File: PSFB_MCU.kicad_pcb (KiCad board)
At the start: 6 copper layers, 38.5 x 33 mm, 104 parts, among them J2 2-215079-0, J3 Conn_01x16, J4 Conn_01x16, U1 APM32F405RGT6, U10 LMV321, U11 LMV321, U12 FM25W256, U13 LMV321, U14 LMV321, U15 LMV321, U16 LMV321, U2 LM2594HVM-3.3, Y1 CSTCE8M00G55A-R0

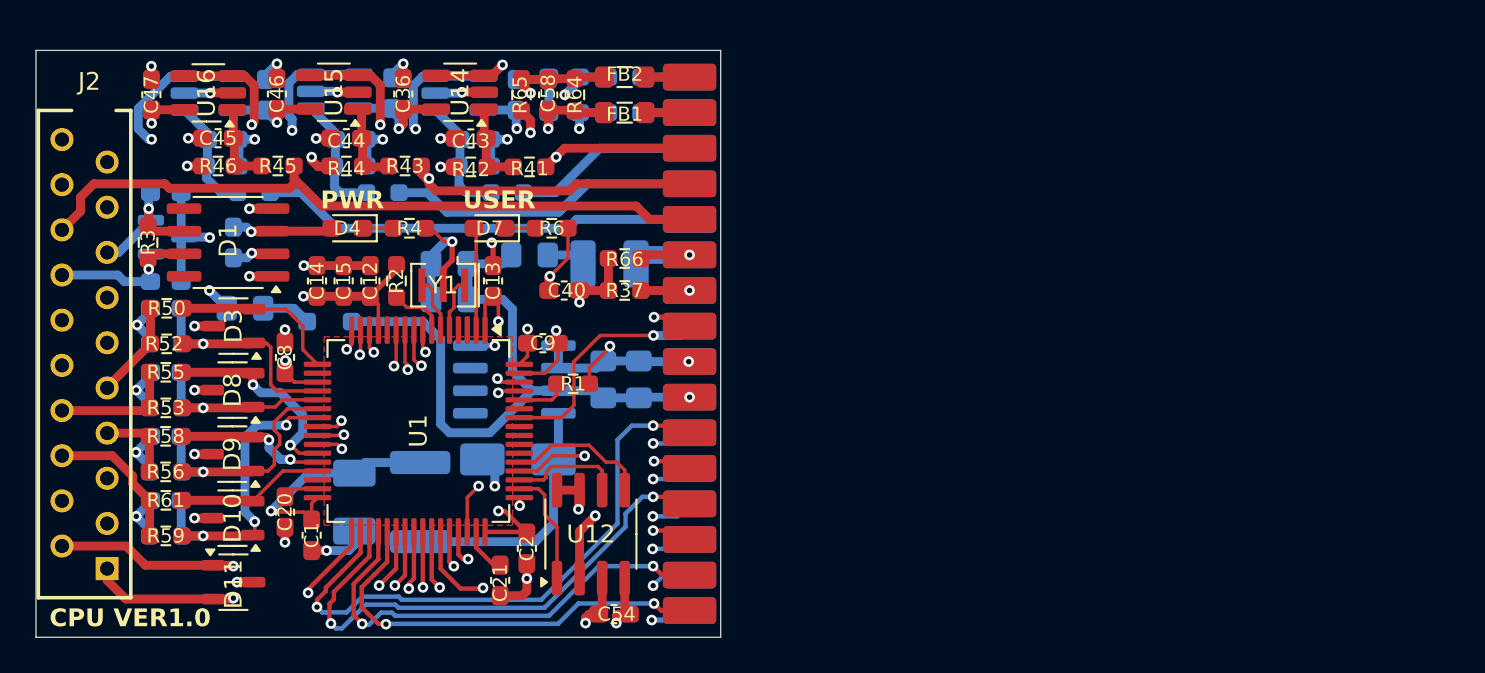
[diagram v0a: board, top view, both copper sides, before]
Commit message: VER1.0: убрал лишнее, добавил на схему питание 5В
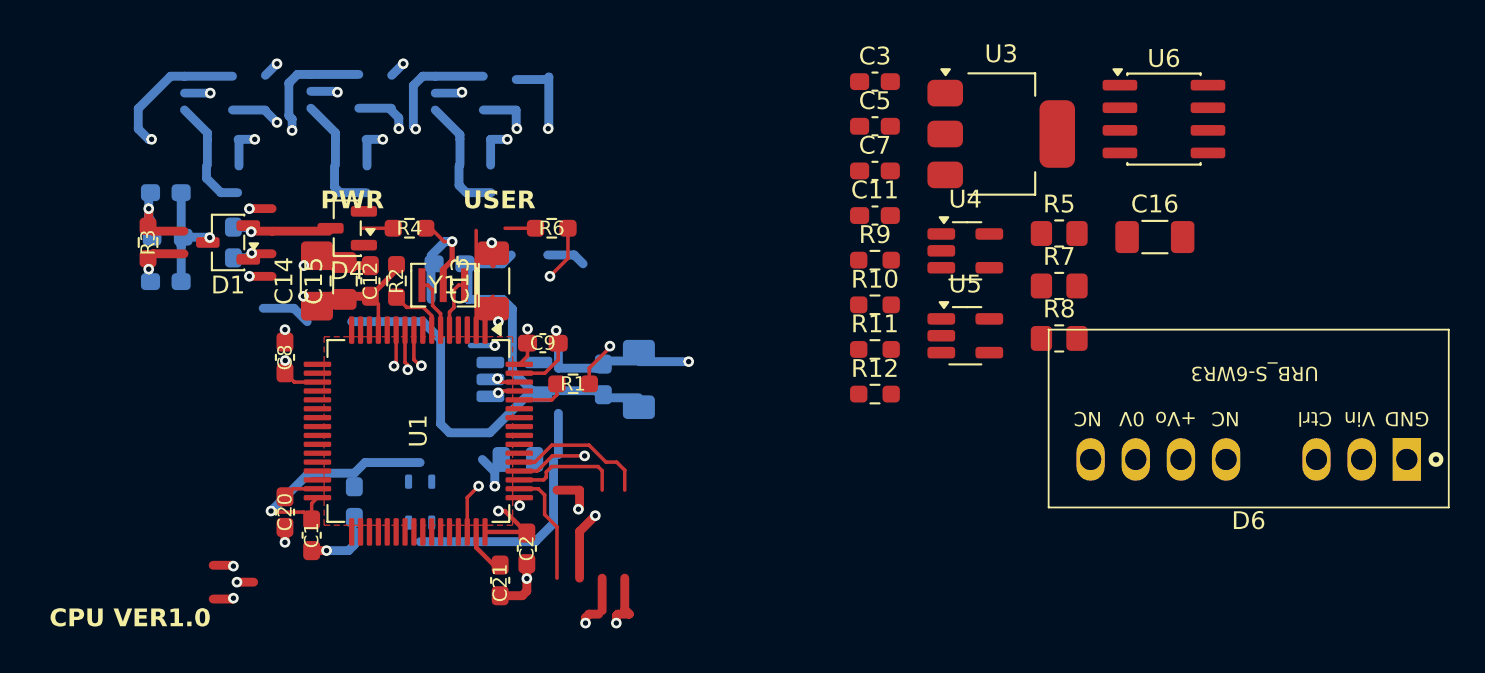
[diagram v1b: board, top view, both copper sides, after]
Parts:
- removed C23: 10u, Capacitor_SMD:C_0805_2012Metric_Pad1.18x1.45mm_HandSolder
- removed C33, C34, C35, C36, C46, C47, C51, C52, C53, C55, C56, C57: 100n, Capacitor_SMD:C_0603_1608Metric_Pad1.08x0.95mm_HandSolder
- removed C37, C39, C40, C41, C43, C44, C45: 1n, Capacitor_SMD:C_0603_1608Metric_Pad1.08x0.95mm_HandSolder
- removed C54: 1u, Capacitor_SMD:C_0603_1608Metric_Pad1.08x0.95mm_HandSolder
- removed C58: 2.2u, Capacitor_SMD:C_0603_1608Metric_Pad1.08x0.95mm_HandSolder
- removed D10, D11, D3, D8, D9: GSOT03C-E3-08, Package_TO_SOT_SMD:SOT-23-3
- removed D7: ~, LED_SMD:LED_0603_1608Metric_Pad1.05x0.95mm_HandSolder
- removed F1, F2: Fuse_Small, Fuse:Fuse_0805_2012Metric_Pad1.15x1.40mm_HandSolder
- removed FB1, FB2: BLM21AG102SN1D, Inductor_SMD:L_0805_2012Metric_Pad1.05x1.20mm_HandSolder
- removed J2: 2-215079-0, TE_my:22150790
- removed J3, J4: Conn_01x16, PLD_my:PLD16_2.0mm
- removed L2: 2.2u, Inductor_SMD:L_1210_3225Metric_Pad1.42x2.65mm_HandSolder
- removed R32, R35, R38, R41, R43, R45, R50, R52, R53, R55, R56, R58, R59, R61, R65: 1.8k, Resistor_SMD:R_0603_1608Metric_Pad0.98x0.95mm_HandSolder
- removed R34, R36, R37, R39, R42, R44, R46, R51, R54, R57, R60, R62, R63, R66: 3.6k, Resistor_SMD:R_0603_1608Metric_Pad0.98x0.95mm_HandSolder
- removed R64: 3.3k, Resistor_SMD:R_0603_1608Metric_Pad0.98x0.95mm_HandSolder
- removed U10, U11, U13, U14, U15, U16: LMV321, Package_TO_SOT_SMD:SOT-23-5_HandSoldering
- removed U12: FM25W256, Package_SO:SOIC-8_3.9x4.9mm_P1.27mm
- added C11: 100n, Capacitor_SMD:C_0603_1608Metric_Pad1.08x0.95mm_HandSolder, F.Cu at (173.7, 91.8)
- added C16: 10u, Capacitor_SMD:C_1206_3216Metric_Pad1.33x1.80mm_HandSolder, F.Cu at (189.4, 93.0)
- added C3: 100n, Capacitor_SMD:C_0603_1608Metric_Pad1.08x0.95mm_HandSolder, F.Cu at (173.7, 84.3)
- added C5: 100n, Capacitor_SMD:C_0603_1608Metric_Pad1.08x0.95mm_HandSolder, F.Cu at (173.7, 86.8)
- added C7: 4.7u, Capacitor_SMD:C_0603_1608Metric_Pad1.08x0.95mm_HandSolder, F.Cu at (173.7, 89.3)
- added R10: 3.6k, Resistor_SMD:R_0603_1608Metric_Pad0.98x0.95mm_HandSolder, F.Cu at (173.7, 96.8)
- added R11: 1.8k, Resistor_SMD:R_0603_1608Metric_Pad0.98x0.95mm_HandSolder, F.Cu at (173.7, 99.3)
- added R12: 3.6k, Resistor_SMD:R_0603_1608Metric_Pad0.98x0.95mm_HandSolder, F.Cu at (173.7, 101.8)
- added R5: 59, Resistor_SMD:R_0805_2012Metric_Pad1.20x1.40mm_HandSolder, F.Cu at (184.0, 92.8)
- added R7: 59, Resistor_SMD:R_0805_2012Metric_Pad1.20x1.40mm_HandSolder, F.Cu at (184.0, 95.7)
- added R8: 750, Resistor_SMD:R_0805_2012Metric_Pad1.20x1.40mm_HandSolder, F.Cu at (184.0, 98.7)
- added R9: 1.8k, Resistor_SMD:R_0603_1608Metric_Pad0.98x0.95mm_HandSolder, F.Cu at (173.7, 94.3)
- added U3: TLV1117LV33DCYR, Package_TO_SOT_SMD:SOT-223-3_TabPin2, F.Cu at (180.8, 87.2)
- added U4: ~, Package_TO_SOT_SMD:SOT-23-5_HandSoldering, F.Cu at (178.8, 93.8)
- added U5: ~, Package_TO_SOT_SMD:SOT-23-5_HandSoldering, F.Cu at (178.8, 98.5)
- added U6: ~, Package_SO:SOIC-8_3.9x4.9mm_P1.27mm, F.Cu at (189.9, 86.4)
- C10: value 56p -> 2.2u
- C12: value 100n -> 1n
- C13: value 100n -> 10u; footprint Capacitor_SMD:C_0603_1608Metric_Pad1.08x0.95mm_HandSolder -> Capacitor_SMD:C_1206_3216Metric_Pad1.33x1.80mm_HandSolder
- C14: value 4.7u -> 0.1u; footprint Capacitor_SMD:C_0603_1608Metric_Pad1.08x0.95mm_HandSolder -> Capacitor_SMD:C_1206_3216Metric_Pad1.33x1.80mm_HandSolder
- C15: value 1u -> 10n; footprint Capacitor_SMD:C_0603_1608Metric_Pad1.08x0.95mm_HandSolder -> Capacitor_SMD:C_0805_2012Metric_Pad1.18x1.45mm_HandSolder
- C17: footprint Capacitor_SMD:C_0805_2012Metric_Pad1.18x1.45mm_HandSolder -> Capacitor_SMD:C_1206_3216Metric_Pad1.33x1.80mm_HandSolder
- C18: value 10u -> 100n; footprint Capacitor_SMD:C_0805_2012Metric_Pad1.18x1.45mm_HandSolder -> Capacitor_SMD:C_0603_1608Metric_Pad1.08x0.95mm_HandSolder
- C19: value 100u -> 1n; footprint Capacitor_Tantalum_SMD:CP_EIA-3528-21_Kemet-B_HandSolder -> Capacitor_SMD:C_0603_1608Metric_Pad1.08x0.95mm_HandSolder
- C20, C6: value 2.2u -> 100n
- C21: value 2.2u -> 1n
- C22: value 10u -> 1u; footprint Capacitor_SMD:C_0805_2012Metric_Pad1.18x1.45mm_HandSolder -> Capacitor_SMD:C_0603_1608Metric_Pad1.08x0.95mm_HandSolder
- C4: value 56p -> 100n
- C8: value 100n -> 1u
- C9: value 100n -> 2.2u
- D1: footprint Package_SO:SOIC-8_3.9x4.9mm_P1.27mm -> Package_TO_SOT_SMD:SOT-23-3
- D2: footprint Package_TO_SOT_SMD:SOT-23 -> LED_SMD:LED_0603_1608Metric_Pad1.05x0.95mm_HandSolder
- D4: footprint LED_SMD:LED_0603_1608Metric_Pad1.05x0.95mm_HandSolder -> Package_TO_SOT_SMD:SOT-23
- D5: value MBRA320 -> ~; footprint Diode_SMD:D_SMA -> LED_SMD:LED_0805_2012Metric
- D6: value D_Schottky_Small -> ~; footprint Diode_SMD:D_SOD-323_HandSoldering -> MORNSUN:URB_S-6WR3; moved to F.Cu
- L1: value 47u -> ~; footprint Inductor_SMD:L_1812_4532Metric_Pad1.30x3.40mm_HandSolder -> Inductor_SMD:L_CommonModeChoke_TDK_ACM2520-2P
- R3: value 120 -> 1k
- R4: value 750 -> 1.8k
- R6: value 1k -> 3.6k
- U1: value APM32F405RGT6 -> ~
- U2: value LM2594HVM-3.3 -> ~; footprint Package_SO:SOIC-8_3.9x4.9mm_P1.27mm -> Package_TO_SOT_SMD:SOT-23-5_HandSoldering
- Y1: value CSTCE8M00G55A-R0 -> ~
- moved D6 52.3 mm to (194.7, 105.5), turned to 180 degrees
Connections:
- C10 pad 1: CANL -> Net-(U1-VCAP_2)
- C12 pad 1: +3.3V -> Net-(U2-+)
- C15 pad 1: +3.3V -> Net-(C15-Pad1)
- C15 pad 2: GND -> GND_CAN
- C17 pad 1: +5V -> GND
- C17 pad 2: GND -> +3.3V
- C18 pad 1: +5V -> +3.3V
- C19 pad 1: +3.3V -> Net-(U4-+)
- C20 pad 1: Net-(U1-VCAP_1) -> +3.3V
- C21 pad 1: Net-(U1-VCAP_2) -> Net-(U5-+)
- C22 pad 1: +5V -> +3.3V
- C4 pad 1: GND -> +3.3V
- C4 pad 2: CANH -> GND
- C6 pad 1: GND -> +3.3V
- C6 pad 2: +3.3V -> GND
- C9 pad 1: +3.3V -> Net-(U1-VCAP_1)
- D1 pad 1: CAN1_TXD_MCU -> SWCLK
- D1 pad 2: GND -> SWDIO
- D1 pad 3: +3.3V -> GND
- D2 pad 1: CANH -> Net-(D2-K)
- D2 pad 2: CANL -> Net-(D2-A)
- D4 pad 1: Net-(D4-K) -> CANH
- D4 pad 2: +3.3V -> CANL
- D5 pad 2: GND -> +3.3V
- D6 pad 1: Net-(D6-K) -> unconnected-(D6-GND-Pad1)
- D6 pad 2: +5V -> unconnected-(D6-Vin-Pad2)
- L1 pad 1: Net-(D5-K) -> Net-(D3-CANH)
- L1 pad 2: +3.3V -> Net-(D3-CANL)
- R3 pad 1: CANL -> Net-(D2-K)
- R3 pad 2: CANH -> GND
- R4 pad 1: Net-(D4-K) -> Current_A
- R4 pad 2: GND -> Net-(U2-+)
- R6 pad 1: Net-(D7-K) -> Net-(U2-+)
- U1 pad 2: Net-(D7-A) -> Net-(D2-A)
- U2 pad 1: unconnected-(U2-NC-Pad1) -> Net-(U2-+)
- U2 pad 2: unconnected-(U2-NC-Pad2) -> GND
- U2 pad 3: unconnected-(U2-NC-Pad3) -> Current_A_MCU
- U2 pad 4: +3.3V -> Current_A_MCU
- U2 pad 5: GND -> +3.3V
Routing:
- net +5V_sense: track 63.6 -> 0.00 mm, vias 2 -> 0
- net Hall2: track 45.8 -> 0.00 mm, vias 1 -> 0
- net Hall1: track 42.2 -> 0.00 mm, vias 1 -> 0
- net Hall3: track 39.0 -> 0.00 mm
- net VBAT_sense_MCU: track 35.9 -> 0.00 mm, vias 2 -> 0
- net Temp_mosfet_sense_MCU: track 34.2 -> 0.00 mm, vias 2 -> 0
- net PWM1_L: track 33.7 -> 0.00 mm, vias 2 -> 0
- net BkIN: track 33.2 -> 0.00 mm, vias 2 -> 0
- net GND: track 108.6 -> 75.5 mm, vias 41 -> 25
- net Temp_motor_sense_MCU: track 32.3 -> 0.00 mm, vias 2 -> 0
- net PWM2_L: track 30.2 -> 0.00 mm, vias 2 -> 0
- net (no net): track 0.00 -> 27.8 mm
- net Hall3_MCU: track 26.1 -> 0.00 mm, vias 2 -> 0
- net PWM3_L: track 26.1 -> 0.00 mm, vias 2 -> 0
- net Hall1_MCU: track 25.0 -> 0.00 mm, vias 2 -> 0
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- removed copper zone on In3.Cu, net +3.3V
- removed copper zone on In4.Cu, net GND
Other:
- board outline removed
- copper layers 6 -> 4

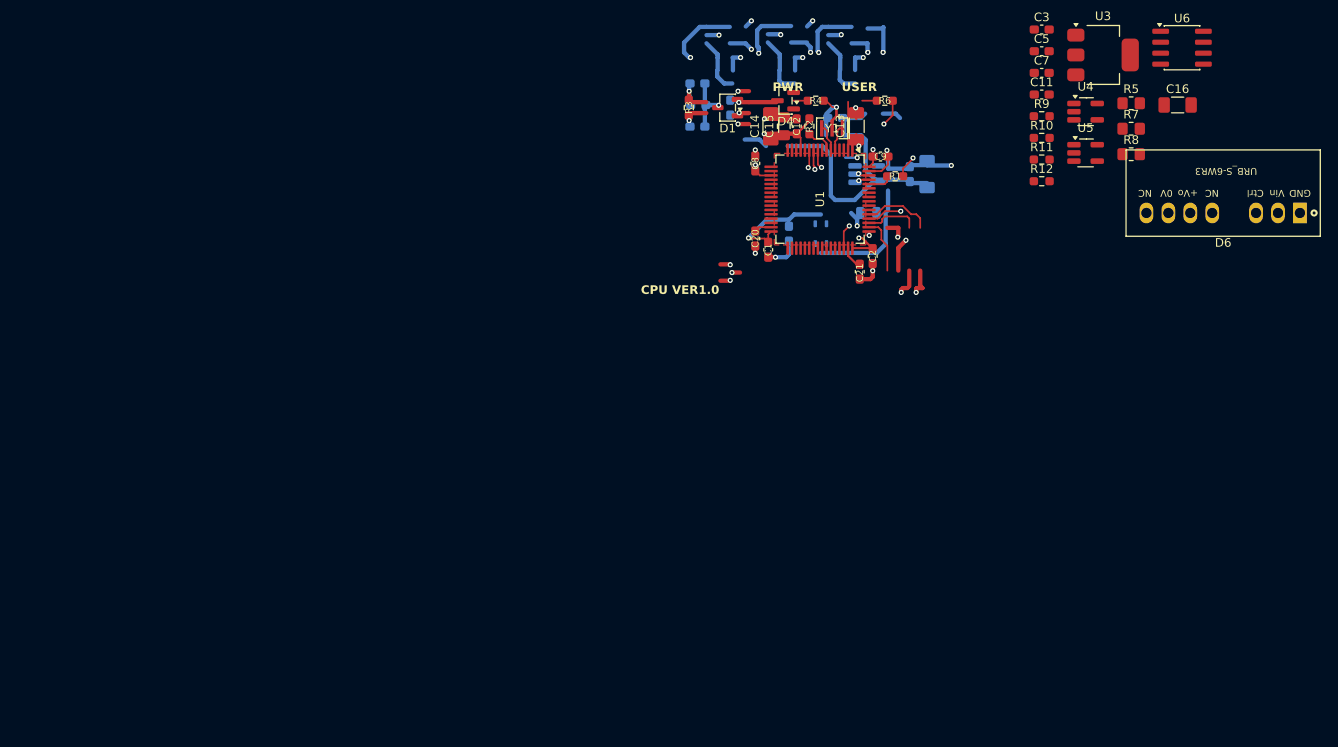
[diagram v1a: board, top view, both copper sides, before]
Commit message: VER1.0: собрал всю цепь питания на схеме
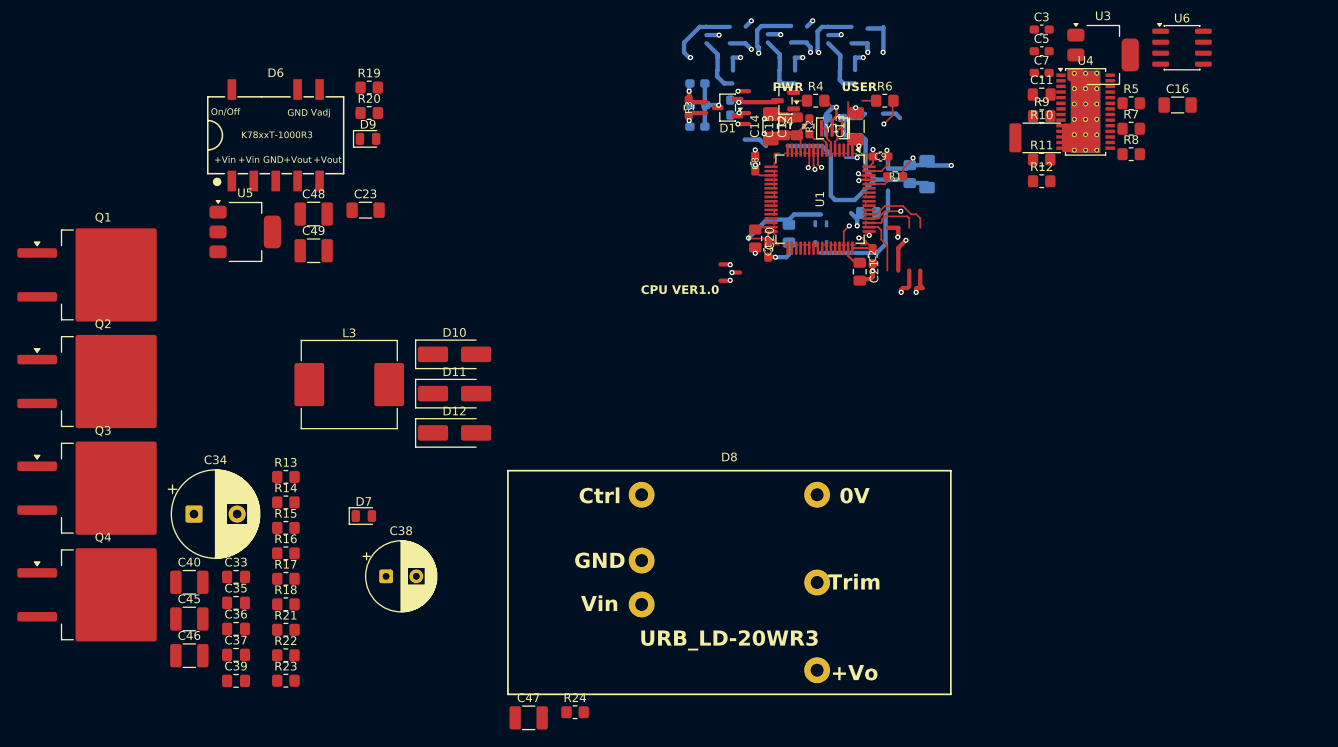
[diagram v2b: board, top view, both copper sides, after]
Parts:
- removed U2: ~, Package_TO_SOT_SMD:SOT-23-5_HandSoldering
- added C23: 10u, Capacitor_SMD:C_1206_3216Metric_Pad1.33x1.80mm_HandSolder, F.Cu at (95.4, 105.2)
- added C33: 560p, Capacitor_SMD:C_0805_2012Metric_Pad1.18x1.45mm_HandSolder, F.Cu at (80.4, 147.7)
- added C34: 100u, Capacitor_THT:CP_Radial_D10.0mm_P5.00mm, F.Cu at (75.5, 140.4)
- added C35: 100n, Capacitor_SMD:C_0805_2012Metric_Pad1.18x1.45mm_HandSolder, F.Cu at (80.4, 150.7)
- added C36: 100n, Capacitor_SMD:C_0805_2012Metric_Pad1.18x1.45mm_HandSolder, F.Cu at (80.4, 153.7)
- added C37: 100n, Capacitor_SMD:C_0805_2012Metric_Pad1.18x1.45mm_HandSolder, F.Cu at (80.4, 156.7)
- added C38: 220u, Capacitor_THT:CP_Radial_D8.0mm_P3.50mm, F.Cu at (97.7, 147.6)
- added C39: 100n, Capacitor_SMD:C_0805_2012Metric_Pad1.18x1.45mm_HandSolder, F.Cu at (80.4, 159.7)
- added C40: 4.7u, Capacitor_SMD:C_1210_3225Metric_Pad1.33x2.70mm_HandSolder, F.Cu at (75.0, 148.3)
- added C45: 10u, Capacitor_SMD:C_1210_3225Metric_Pad1.33x2.70mm_HandSolder, F.Cu at (75.0, 152.5)
- added C46: 10u, Capacitor_SMD:C_1210_3225Metric_Pad1.33x2.70mm_HandSolder, F.Cu at (75.0, 156.8)
- added C47: 10u, Capacitor_SMD:C_1210_3225Metric_Pad1.33x2.70mm_HandSolder, F.Cu at (114.3, 164.0)
- added C48: 10u, Capacitor_SMD:C_1210_3225Metric_Pad1.33x2.70mm_HandSolder, F.Cu at (89.4, 105.6)
- added C49: 10u, Capacitor_SMD:C_1210_3225Metric_Pad1.33x2.70mm_HandSolder, F.Cu at (89.4, 109.9)
- added D10: D_Schottky_Small, Diode_SMD:D_SMA_Handsoldering, F.Cu at (105.7, 121.9)
- added D11: D_Schottky_Small, Diode_SMD:D_SMA_Handsoldering, F.Cu at (105.7, 126.4)
- added D12: D_Schottky_Small, Diode_SMD:D_SMA_Handsoldering, F.Cu at (105.7, 131.0)
- added D7: ~, LED_SMD:LED_0805_2012Metric, F.Cu at (95.2, 140.6)
- added D8: URB2415LD-20WR3, MORNSUN:URB_LD-20WR3, F.Cu at (137.5, 148.3)
- added D9: ~, LED_SMD:LED_0805_2012Metric, F.Cu at (95.7, 96.9)
- added L3: 10u, Inductor_SMD:L_Panasonic_PCC-M1040ML, F.Cu at (93.5, 125.4)
- added Q1: WMM043N10HGD, Package_TO_SOT_SMD:TO-263-2, F.Cu at (65.0, 112.7)
- added Q2: WMM043N10HGD, Package_TO_SOT_SMD:TO-263-2, F.Cu at (65.0, 125.0)
- added Q3: WMM043N10HGD, Package_TO_SOT_SMD:TO-263-2, F.Cu at (65.0, 137.4)
- added Q4: WMM043N10HGD, Package_TO_SOT_SMD:TO-263-2, F.Cu at (65.0, 149.7)
- added R13: 59k, Resistor_SMD:R_0805_2012Metric_Pad1.20x1.40mm_HandSolder, F.Cu at (86.1, 136.1)
- added R14: 249k, Resistor_SMD:R_0805_2012Metric_Pad1.20x1.40mm_HandSolder, F.Cu at (86.1, 139.0)
- added R15: 10, Resistor_SMD:R_0805_2012Metric_Pad1.20x1.40mm_HandSolder, F.Cu at (86.1, 142.0)
- added R16: 2k, Resistor_SMD:R_0805_2012Metric_Pad1.20x1.40mm_HandSolder, F.Cu at (86.1, 144.9)
- added R17: 10k, Resistor_SMD:R_0805_2012Metric_Pad1.20x1.40mm_HandSolder, F.Cu at (86.1, 147.9)
- added R18: 0, Resistor_SMD:R_0805_2012Metric_Pad1.20x1.40mm_HandSolder, F.Cu at (86.1, 150.8)
- added R19: 1k, Resistor_SMD:R_0805_2012Metric_Pad1.20x1.40mm_HandSolder, F.Cu at (95.8, 91.0)
- added R20: 3k, Resistor_SMD:R_0805_2012Metric_Pad1.20x1.40mm_HandSolder, F.Cu at (95.8, 93.9)
- added R21: 10k, Resistor_SMD:R_0805_2012Metric_Pad1.20x1.40mm_HandSolder, F.Cu at (86.1, 153.8)
- added R22: 240k, Resistor_SMD:R_0805_2012Metric_Pad1.20x1.40mm_HandSolder, F.Cu at (86.1, 156.7)
- added R23: 51k, Resistor_SMD:R_0805_2012Metric_Pad1.20x1.40mm_HandSolder, F.Cu at (86.1, 159.7)
- added R24: 0, Resistor_SMD:R_0805_2012Metric_Pad1.20x1.40mm_HandSolder, F.Cu at (119.6, 163.3)
- C11: value 100n -> 1u; footprint Capacitor_SMD:C_0603_1608Metric_Pad1.08x0.95mm_HandSolder -> Capacitor_SMD:C_0805_2012Metric_Pad1.18x1.45mm_HandSolder
- C12: value 1n -> 220p; footprint Capacitor_SMD:C_0603_1608Metric_Pad1.08x0.95mm_HandSolder -> Capacitor_SMD:C_0805_2012Metric_Pad1.18x1.45mm_HandSolder
- C18: footprint Capacitor_SMD:C_0603_1608Metric_Pad1.08x0.95mm_HandSolder -> Capacitor_SMD:C_0805_2012Metric_Pad1.18x1.45mm_HandSolder
- C19: value 1n -> 47p; footprint Capacitor_SMD:C_0603_1608Metric_Pad1.08x0.95mm_HandSolder -> Capacitor_SMD:C_0805_2012Metric_Pad1.18x1.45mm_HandSolder
- C20: value 100n -> 1n; footprint Capacitor_SMD:C_0603_1608Metric_Pad1.08x0.95mm_HandSolder -> Capacitor_SMD:C_0805_2012Metric_Pad1.18x1.45mm_HandSolder
- C21: value 1n -> 33n; footprint Capacitor_SMD:C_0603_1608Metric_Pad1.08x0.95mm_HandSolder -> Capacitor_SMD:C_0805_2012Metric_Pad1.18x1.45mm_HandSolder
- D6: value ~ -> K7809T; footprint MORNSUN:URB_S-6WR3 -> MORNSUN:K78xxT-1000R3
- R10: value 3.6k -> 10m; footprint Resistor_SMD:R_0603_1608Metric_Pad0.98x0.95mm_HandSolder -> Resistor_SMD:R_2512_6332Metric_Pad1.40x3.35mm_HandSolder
- R11: value 1.8k -> 143k; footprint Resistor_SMD:R_0603_1608Metric_Pad0.98x0.95mm_HandSolder -> Resistor_SMD:R_0805_2012Metric_Pad1.20x1.40mm_HandSolder
- R12: value 3.6k -> 10k; footprint Resistor_SMD:R_0603_1608Metric_Pad0.98x0.95mm_HandSolder -> Resistor_SMD:R_0805_2012Metric_Pad1.20x1.40mm_HandSolder
- R4: value 1.8k -> 93.1k; footprint Resistor_SMD:R_0603_1608Metric_Pad0.98x0.95mm_HandSolder -> Resistor_SMD:R_0805_2012Metric_Pad1.20x1.40mm_HandSolder
- R6: value 3.6k -> 100; footprint Resistor_SMD:R_0603_1608Metric_Pad0.98x0.95mm_HandSolder -> Resistor_SMD:R_0805_2012Metric_Pad1.20x1.40mm_HandSolder
- R8: value 750 -> 1k
- R9: value 1.8k -> 100; footprint Resistor_SMD:R_0603_1608Metric_Pad0.98x0.95mm_HandSolder -> Resistor_SMD:R_0805_2012Metric_Pad1.20x1.40mm_HandSolder
- U3: value TLV1117LV33DCYR -> AMS1117-3.3
- U4: value ~ -> LM5176PWP; footprint Package_TO_SOT_SMD:SOT-23-5_HandSoldering -> Package_SO:HTSSOP-28-1EP_4.4x9.7mm_P0.65mm_EP3.4x9.5mm_ThermalVias
- U5: value ~ -> AMS1117-5.0; footprint Package_TO_SOT_SMD:SOT-23-5_HandSoldering -> Package_TO_SOT_SMD:SOT-223-3_TabPin2
- moved D6 110.1 mm to (85.0, 96.5), turned to 0 degrees
- moved U5 97.8 mm to (81.4, 107.7)
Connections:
- net AnalogIN2_MCU renamed PWM1_L_2
- net AnalogIN3_MCU renamed BkIN_2
- net BkIN renamed BkIN_1
- net DigIN2_MCU renamed PWM3_L_2
- net PWM1_H renamed PWM1_H_1
- net PWM1_L renamed PWM1_L_1
- net PWM2_H renamed PWM2_H_1
- net PWM2_L renamed PWM2_L_1
- net PWM3_H renamed PWM3_H_1
- net PWM3_L renamed PWM3_L_1
- net Temp_mosfet_sense_MCU renamed PWM2_L_2
- net f2H renamed PWM3_H_2
- net f3H renamed PWM2_H_2
- net f3L renamed PWM1_H_2
- C11 pad 1: +3.3V -> VCC
- C11 pad 2: GND -> GND_IN
- C12 pad 1: Net-(U2-+) -> Net-(U4-SLOPE)
- C12 pad 2: GND -> GND_IN
- C18 pad 1: +3.3V -> Net-(U4-SS)
- C18 pad 2: GND -> GND_IN
- C19 pad 1: Net-(U4-+) -> Net-(U4-CSG)
- C19 pad 2: GND -> Net-(U4-CS)
- C20 pad 1: +3.3V -> Net-(U4-RT/SYNC)
- C20 pad 2: GND -> unconnected-(C20-Pad2)
- C21 pad 1: Net-(U5-+) -> Net-(U4-COMP)
- C21 pad 2: GND -> Net-(C21-Pad2)
- D6 pad 1: unconnected-(D6-GND-Pad1) -> +15V
- D6 pad 2: unconnected-(D6-Vin-Pad2) -> +15V
- D6 pad 3: unconnected-(D6-Ctrl-Pad3) -> GND
- D6 pad 5: unconnected-(D6-NC-Pad5) -> +9V
- D6 pad 7: unconnected-(D6-0V-Pad7) -> GND
- L1 pad 2: Net-(D3-CANL) -> CANH
- L1 pad 3: CANL -> Net-(D3-CANL)
- L1 pad 4: CANH -> CANL
- R10 pad 1: Net-(U4-+) -> GND_IN
- R10 pad 2: GND -> Net-(Q2-S)
- R11 pad 1: Current_C -> GND_IN
- R11 pad 2: Net-(U5-+) -> Net-(U4-RT/SYNC)
- R12 pad 1: Net-(U5-+) -> GND_IN
- R12 pad 2: GND -> Net-(C21-Pad2)
- R4 pad 1: Current_A -> GND_IN
- R4 pad 2: Net-(U2-+) -> Net-(U4-MODE)
- R6 pad 1: Net-(U2-+) -> Net-(Q2-S)
- R6 pad 2: GND -> Net-(U4-CS)
- R9 pad 1: Current_B -> GND_IN
- R9 pad 2: Net-(U4-+) -> Net-(U4-CSG)
- U1 pad 10: Current_B_MCU -> unconnected-(U1-PC2-Pad10)
- U1 pad 11: Current_C_MCU -> unconnected-(U1-PC3-Pad11)
- U1 pad 14: Hall3_MCU -> unconnected-(U1-PA0-Pad14)
- U1 pad 15: Hall1_MCU -> unconnected-(U1-PA1-Pad15)
- U1 pad 16: Hall2_MCU -> unconnected-(U1-PA2-Pad16)
- U1 pad 17: DigIN1_MCU -> unconnected-(U1-PA3-Pad17)
- U1 pad 20: AnalogIN1_MCU -> unconnected-(U1-PA4-Pad20)
- U1 pad 23: AnalogIN4_MCU -> unconnected-(U1-PA7-Pad23)
- U1 pad 24: VBAT_sense_MCU -> unconnected-(U1-PC4-Pad24)
- U1 pad 25: Temp_motor_sense_MCU -> unconnected-(U1-PC5-Pad25)
- U1 pad 28: DigIN3_MCU -> unconnected-(U1-PB2-Pad28)
- U1 pad 29: DigIN4_MCU -> unconnected-(U1-PB10-Pad29)
- U1 pad 40: f2L -> unconnected-(U1-PC9-Pad40)
- U1 pad 44: f1H -> unconnected-(U1-PA11-Pad44)
- U1 pad 45: f1L -> unconnected-(U1-PA12-Pad45)
- U1 pad 58: uC_drv_en -> unconnected-(U1-PB6-Pad58)
- U1 pad 8: +5V_sense_MCU -> unconnected-(U1-PC0-Pad8)
- U1 pad 9: Current_A_MCU -> unconnected-(U1-PC1-Pad9)
- U4 pad 1: Net-(U4-+) -> Net-(U4-EN/UVLO)
- U4 pad 2: GND -> Net-(U4-VIN)
- U4 pad 3: Current_B_MCU -> Net-(U4-VISNS)
- U4 pad 4: Current_B_MCU -> Net-(U4-MODE)
- U4 pad 5: +3.3V -> GND_IN
- U5 pad 1: Net-(U5-+) -> GND
- U5 pad 2: GND -> +5V
- U5 pad 3: Current_C_MCU -> +9V
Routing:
- net unconnected-(U1-PC1-Pad9): track 0.00 -> 38.2 mm, vias 0 -> 2
- net Current_A_MCU: track 38.2 -> 0.00 mm, vias 2 -> 0
- net unconnected-(U1-PC2-Pad10): track 0.00 -> 28.2 mm, vias 0 -> 2
- net Current_B_MCU: track 28.2 -> 0.00 mm, vias 2 -> 0
- net unconnected-(U1-PC3-Pad11): track 0.00 -> 22.6 mm, vias 0 -> 2
- net Current_C_MCU: track 22.6 -> 0.00 mm, vias 2 -> 0
- net (no net): track 27.8 -> 45.8 mm, vias 0 -> 1
- net Net-(D5-K): track 13.8 -> 0.00 mm
- net GND: track 75.5 -> 71.6 mm, vias 25 -> 23
- net Net-(U4-CS): track 0.00 -> 3.12 mm, vias 0 -> 1
- net unconnected-(D6-Ctrl-Pad3): track 2.79 -> 0.00 mm
- net Net-(U2-+): track 1.71 -> 0.00 mm
- net Net-(Q2-S): track 0.00 -> 1.71 mm
- net GND_IN: track 0.00 -> 1.71 mm
- net Current_A: track 1.71 -> 0.00 mm
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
